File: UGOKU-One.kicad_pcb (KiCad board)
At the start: 2 copper layers, 70 x 70 mm, 85 parts, among them J1 Conn_01x04, J10 Conn_01x02, J11 USB_C_Receptacle_USB2.0_16P, J12 Conn_01x02, J13 Conn_01x02, J2 SERVO, J3 Conn_02x03_Odd_Even, J4 Conn_01x10, J5 SERVO, J6 Conn_01x02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

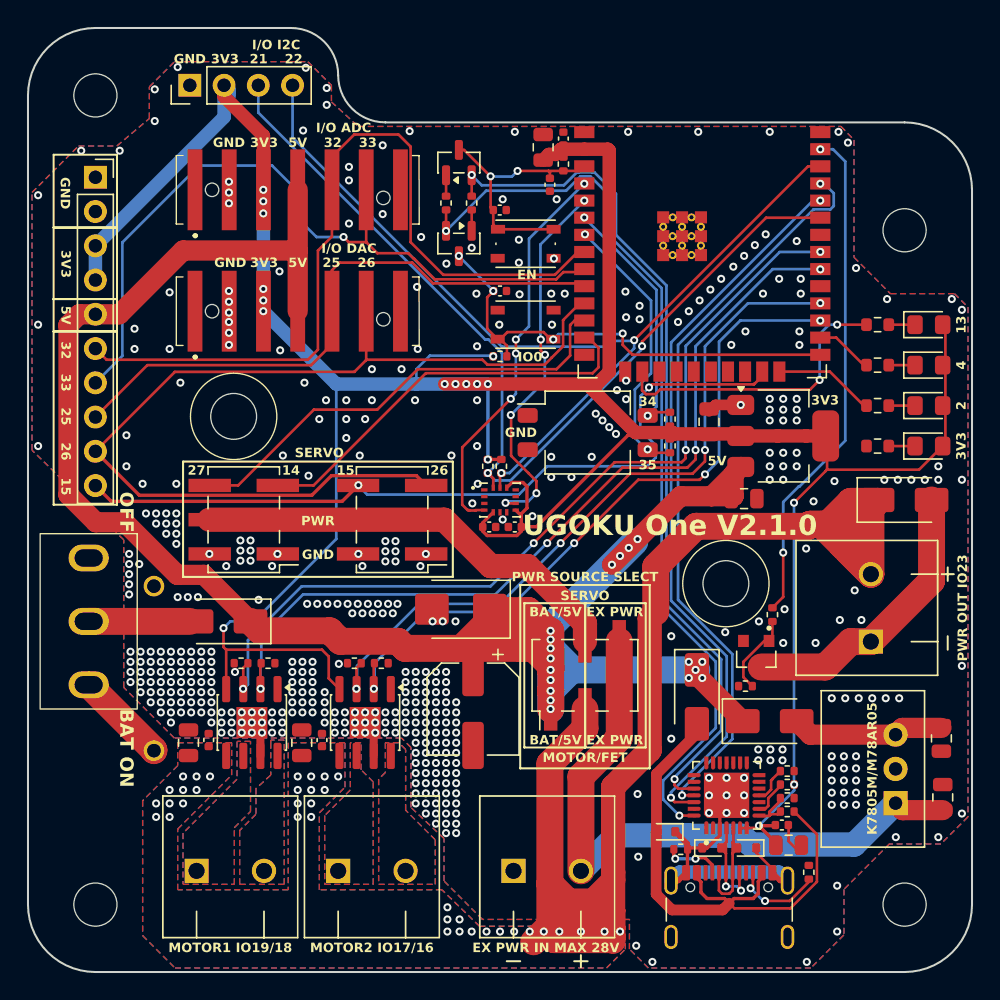
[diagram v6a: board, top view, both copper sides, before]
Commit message: MD周りのベタ, viaを修正 BOM,CPLファイルを整備
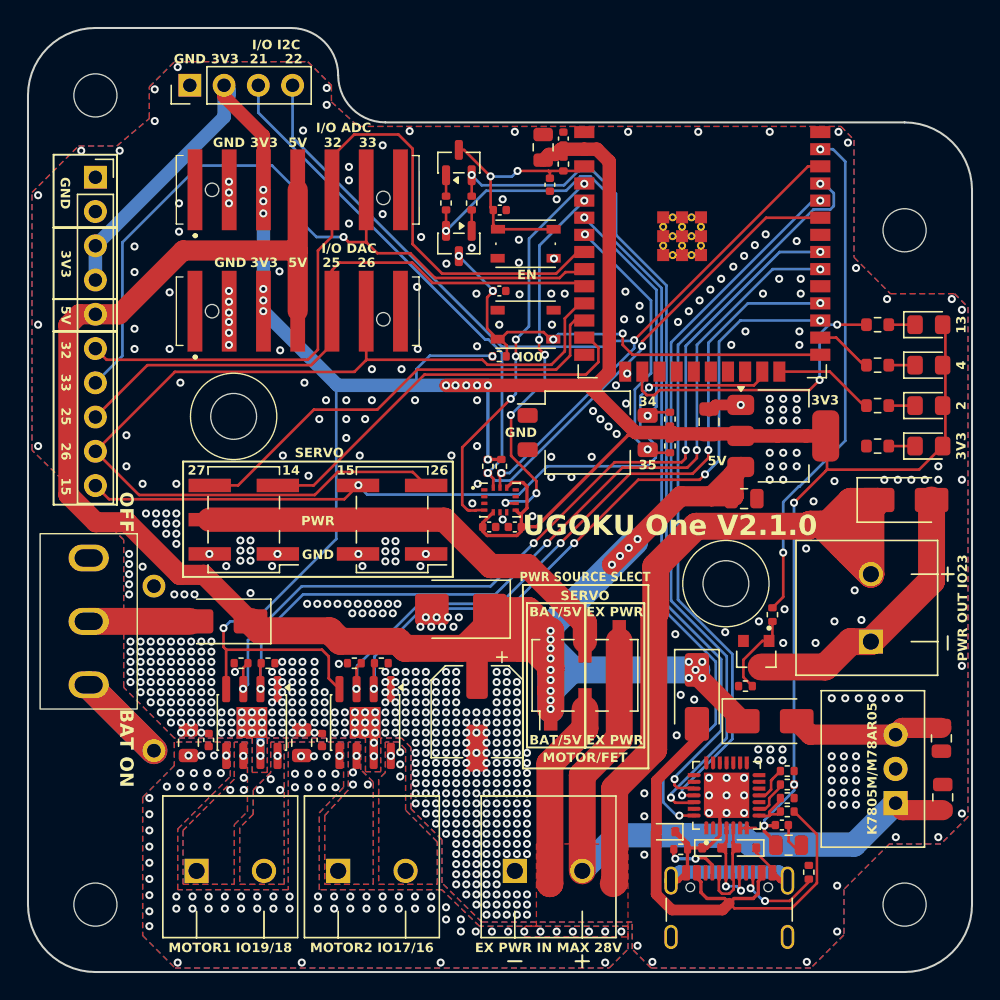
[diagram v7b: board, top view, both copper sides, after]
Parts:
- C12, C20, C21, C3, C7, C8: value 0.1uF -> 0.1μF
- C2: value 22uF -> 22μF
- J2, J5: value SERVO -> Conn_02x03_Odd_Even
- J8: value DAC -> Harting-Conn
- J9: value ADC -> Harting-Conn
- L2: value IO2 -> LED
- moved C4 0.36 mm to (-1.70, 15.7)
- moved J12 0.10 mm to (3.60, 27.5)
- moved C7 0.05 mm to (-0.05, -15.5)
- moved R32 0.05 mm to (-0.05, -10.7)
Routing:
- net MOT_PWR: track 106.8 -> 77.4 mm, vias 37 -> 83
- net Net-(BT1-+): track 6.89 -> 13.8 mm
- net GND: track 32.6 -> 34.4 mm, vias 470 -> 670
- net 3V3: track 236.7 -> 235.3 mm
- net DAC2: track 72.6 -> 73.1 mm
- net Net-(J6-Pin_2): vias 0 -> 4
- net Net-(J6-Pin_1): vias 0 -> 4
- net Net-(J10-Pin_2): vias 0 -> 4
- net Net-(J10-Pin_1): vias 0 -> 4

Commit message: ビアの位置を修正
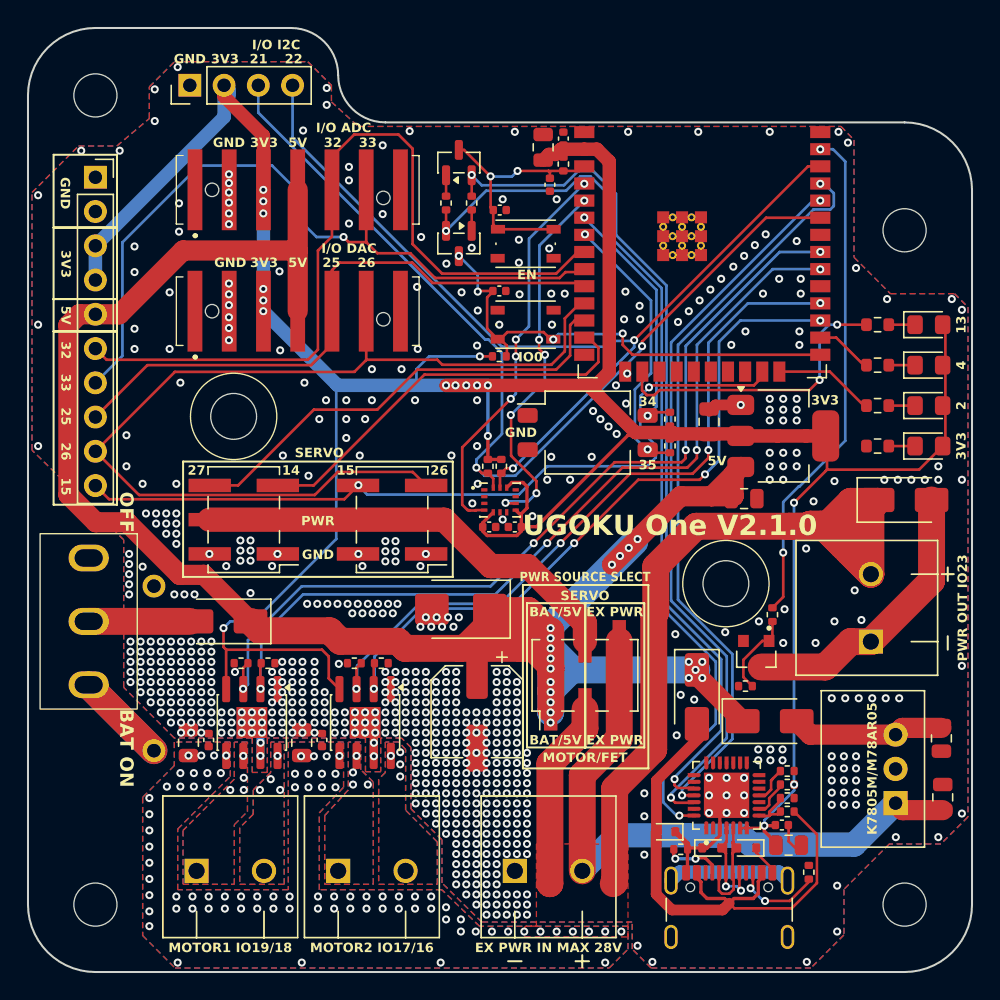
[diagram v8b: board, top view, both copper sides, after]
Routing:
- net MOT_PWR: track 77.4 -> 82.0 mm
- net GND: track 34.4 -> 31.7 mm, vias 670 -> 674
- net SDA: track 71.3 -> 73.0 mm
- net IO0: track 34.9 -> 35.6 mm
- net 3V3: track 235.3 -> 236.0 mm
- net 5V: track 158.9 -> 159.1 mm, vias 18 -> 19
